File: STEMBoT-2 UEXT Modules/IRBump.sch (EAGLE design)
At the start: 21 parts, among them IC1 LMV324DR2G, IC2 LMV324DR2G, IC3 74HC165PW,118, Q1 MMBT3904LP-7

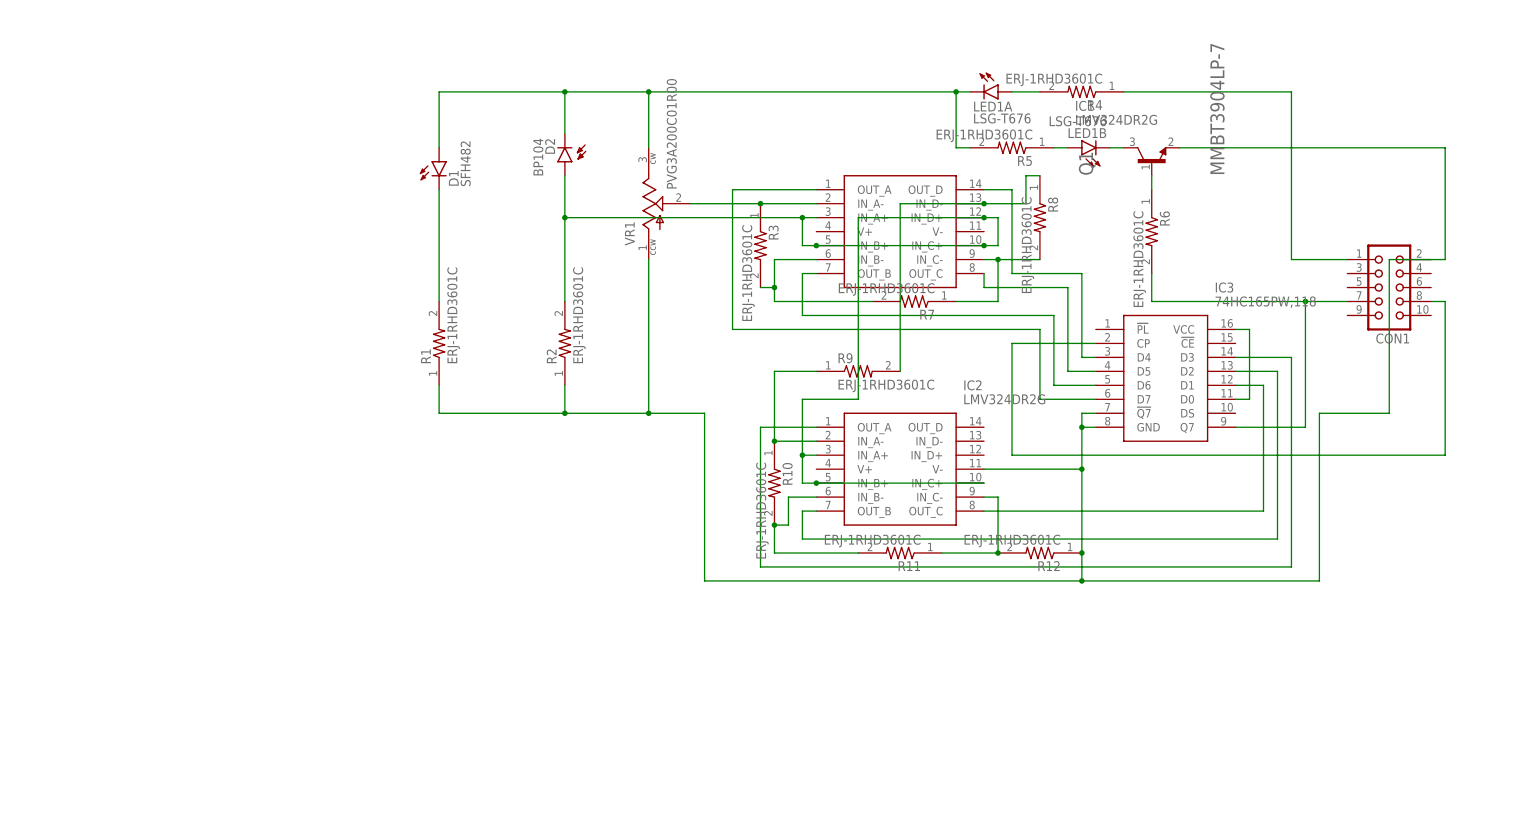
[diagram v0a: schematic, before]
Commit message: Adjusted ADC modules for PCB order. Dan, these are auto-routed.
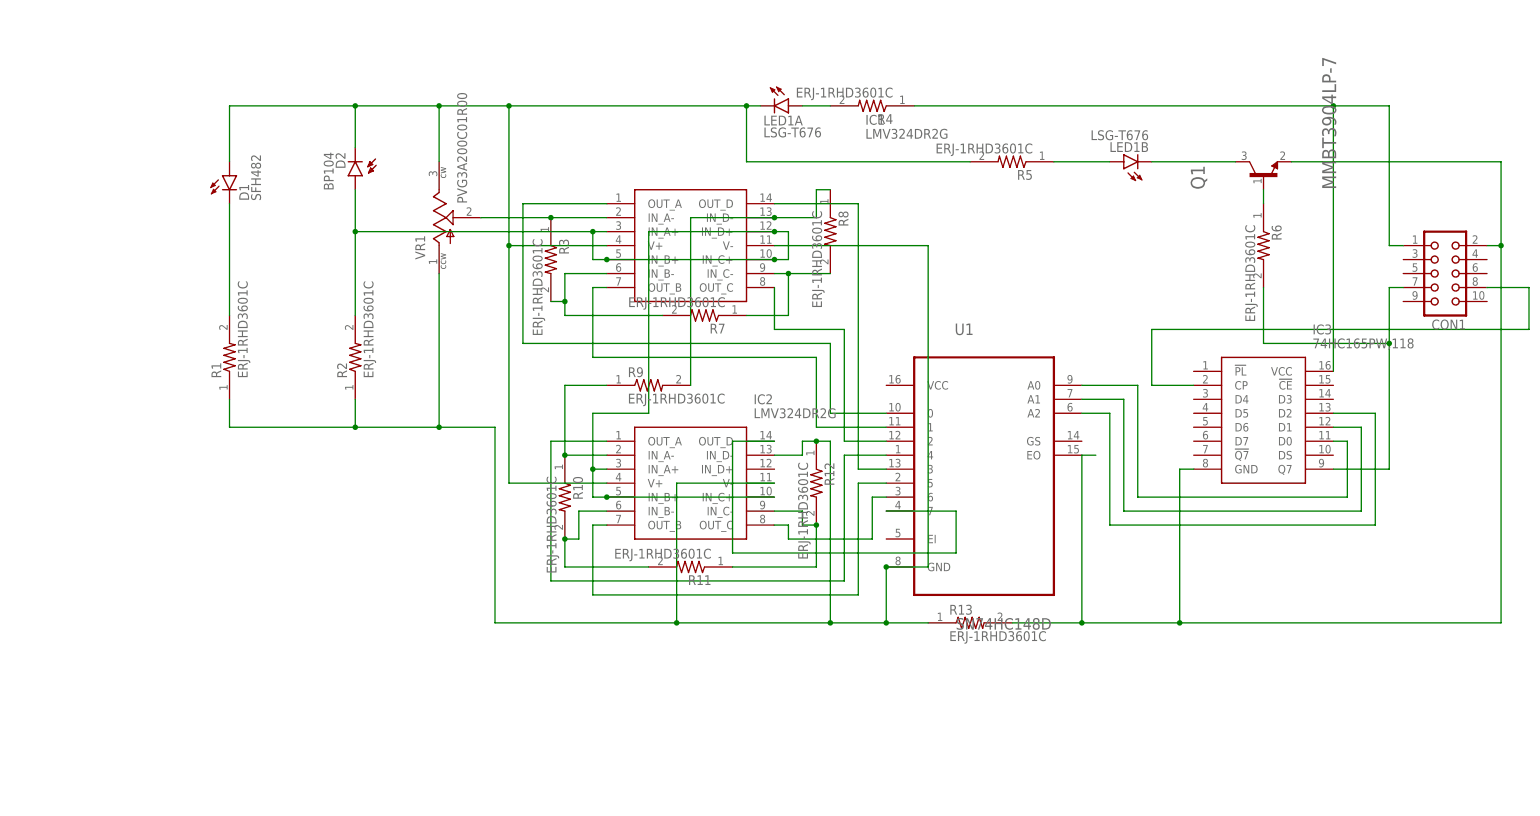
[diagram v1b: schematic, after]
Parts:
- added R13: ERJ-1RHD3601C, Resistor:ERJ-1RHD3601C
- added U1: SN74HC148D, SN74HC148D:SN74HC148D
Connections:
- removed net N$26 (its old number): IC3.D0, IC3.VCC
- new net N$21: IC1.V-, IC2.IN_D-, IC2.V-, R1.1, R12.1, R13.1, R2.1, U1.GND, VR1.CCW
- new net N$28: IC3.D0, U1.A0
- new net N$29: IC3.D1, U1.A1
- new net N$30: IC3.D2, U1.A2
- new net N$4: CON1.2, IC3.GND, Q1.E, R13.2, U1.EO
- net N$1: now also IC2.OUT_C, U1.6; no longer CON1.2, IC2.V-, IC3.!Q7, IC3.GND, Q1.E, R1.1, R12.1, R2.1, VR1.CCW
- net N$11: now also U1.4; no longer IC3.D3
- net N$13: now also U1.5; no longer IC3.D2
- net N$17: now also IC3.VCC
- net N$22: now also U1.3; no longer IC3.D4
- net N$23: now also U1.2; no longer IC3.D5
- net N$24: now also U1.1; no longer IC3.D6
- net N$25: now also U1.0; no longer IC3.D7
- net N$6: now also IC1.V+, IC2.V+
- net N$9: now also IC2.OUT_D, U1.7; no longer IC2.OUT_C, IC3.D1
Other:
- moved on the sheet: CON1, D1, D2, IC1, IC2, IC3, LED1A, LED1B, Q1, R1, R10, R11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

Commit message: Once again, updating ADC shematics and boards. Used autorouter.
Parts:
- removed IC1, IC2: LMV324DR2G, LMV324DR2G:LMV324DR2G
- added R14, R15: ERJ-1RHD3601C, Resistor:ERJ-1RHD3601C
- added U2, U3: MAX964ESET, MAX964ESET:MAX964ESET
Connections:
- removed net N$21: IC1.V-, IC2.IN_D-, IC2.V-, R1.1, R12.1, R13.1, R2.1, U1.GND, VR1.CCW
- new net N$27: U1.2, U3.QB
- new net N$32: U1.1, U3.QC
- new net N$33: U1.0, U3.QD
- net N$1: now also R3.2, U2.INA+, U2.INB+, U2.INC+, U2.IND+, U3.INA+, U3.INB+, U3.INC+, U3.IND+; no longer IC2.OUT_C, U1.6
- net N$11: now also R10.2, R8.1, U2.INB-; no longer IC2.OUT_A, U1.4
- net N$13: now also R12.1, R8.2, U2.INC-; no longer IC2.OUT_B, U1.5
- net N$14: no longer IC1.IN_A-
- net N$15: now also R12.2, R7.1, U2.IND-; no longer IC1.IN_B-, R3.2, R7.2
- net N$16: now also R13.2, R7.2, U3.INA-; no longer IC1.IN_C-, R7.1, R8.2
- net N$18: now also R13.1, U3.INB-; no longer IC1.IN_D-, R8.1
- net N$19: now also R14.2, U3.INC-; no longer IC2.IN_A-, R10.1
- net N$20: now also R14.1, R15.2, U3.IND-; no longer IC2.IN_B-, R10.2, R11.2
- net N$22: now also U1.6, U2.QB; no longer IC1.OUT_D, U1.3
- net N$23: now also U1.5, U2.QC; no longer IC1.OUT_C, U1.2
- net N$24: now also U1.3, U2.QD; no longer IC1.OUT_B, U1.1
- net N$25: now also U1.4, U3.QA; no longer IC1.OUT_A, U1.0
- net N$4: now also R1.1, R15.1, R2.1, U1.GND, U2.GND, U3.GND, VR1.CCW; no longer R13.2, U1.EO
- net N$5: now also U1.7, U2.QA; no longer IC2.IN_C-, R11.1, R12.2
- net N$6: now also R11.1, U1.VCC, U2.VCC, U3.VCC; no longer IC1.V+, IC2.V+
- net N$7: no longer IC1.IN_A+, IC1.IN_B+, IC1.IN_C+, IC1.IN_D+, IC2.IN_A+, IC2.IN_B+, IC2.IN_C+
- net N$9: now also R10.1, R11.2, U2.INA-; no longer IC2.OUT_D, U1.7
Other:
- moved on the sheet: D1, D2, LED1A, R1, R10, R11, R12, R13, R2, R3, R4, R7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
